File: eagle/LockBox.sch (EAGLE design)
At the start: 12 parts

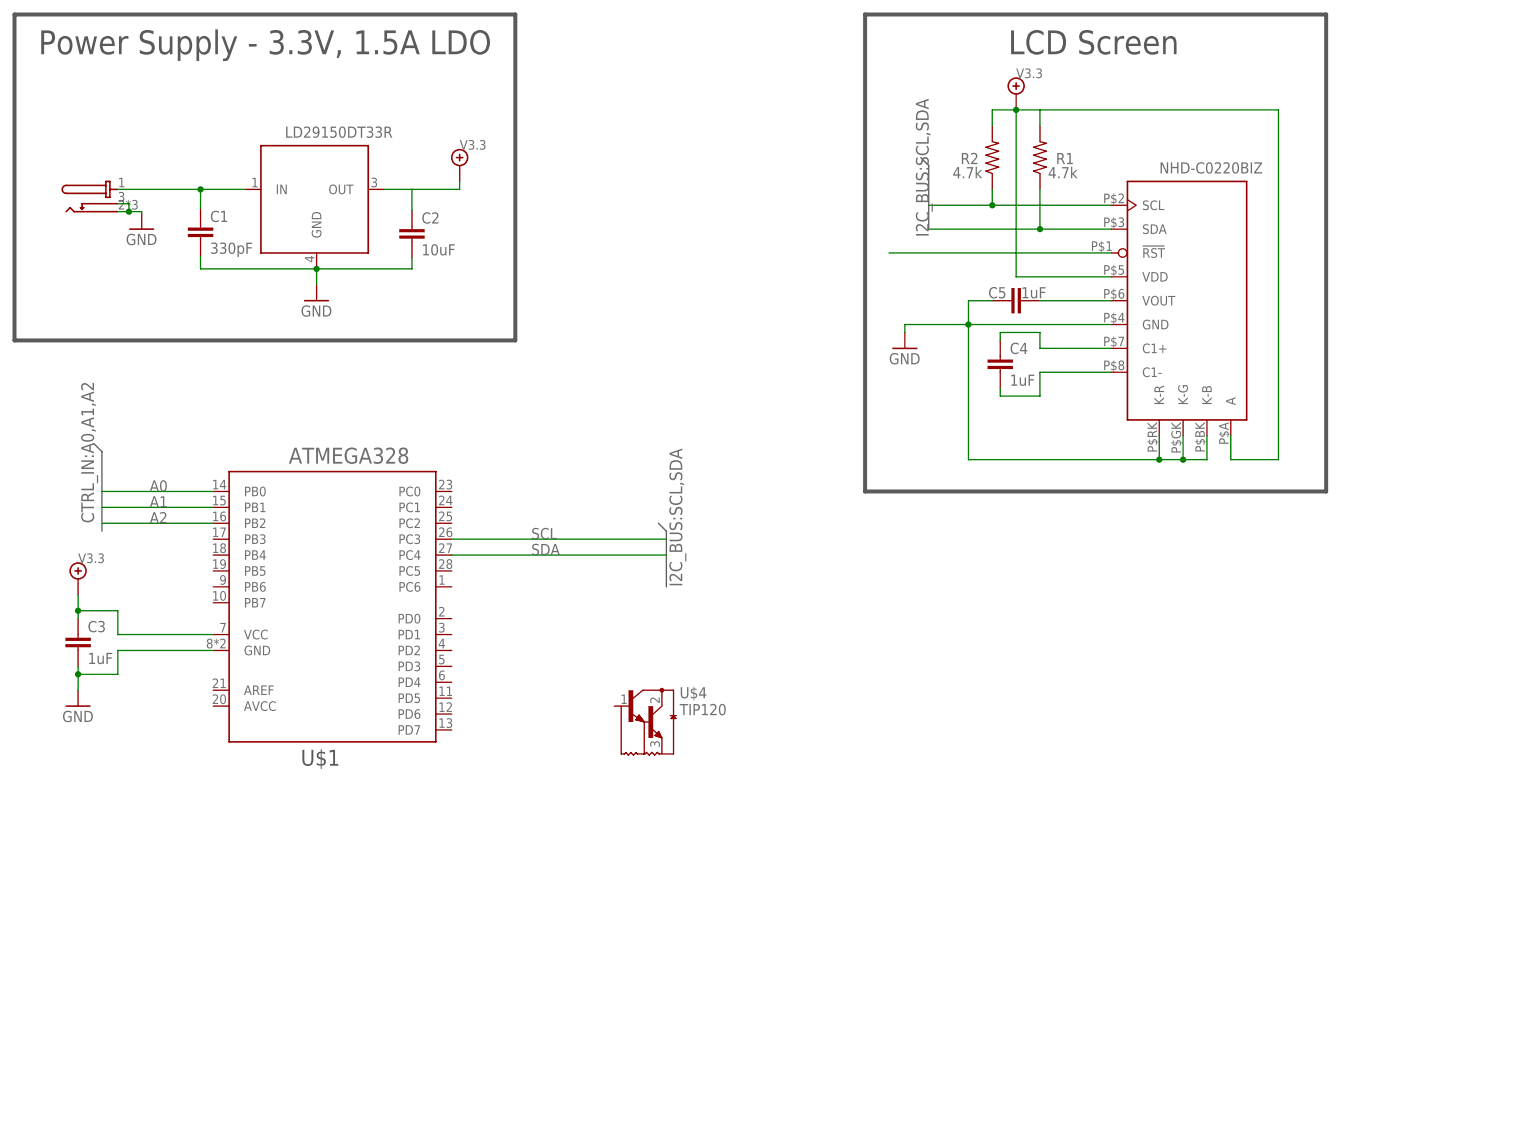
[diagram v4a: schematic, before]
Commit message: Added the TIP120 to LockBox.sch
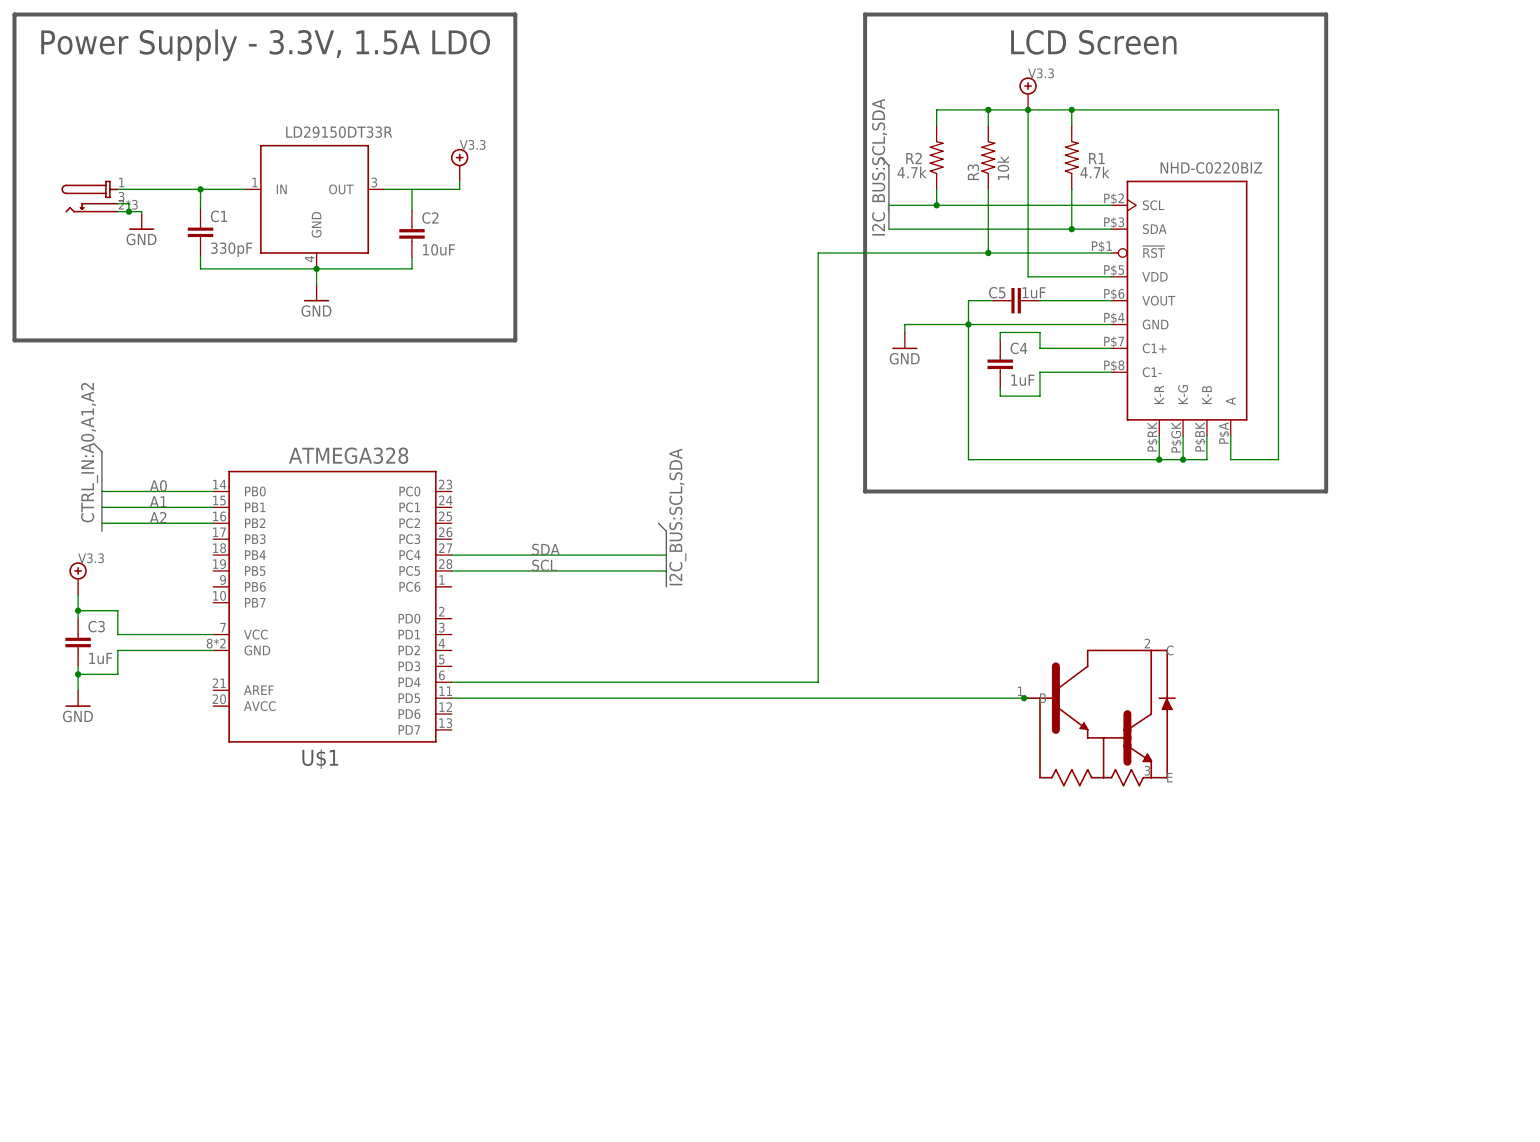
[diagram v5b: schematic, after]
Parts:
- added R3: 10k, LockBox:R-US_M0805
- U$1: PC3 SCL -> (none); PC5 (none) -> SCL; PD4 (none) -> GPIO; PD5 (none) -> GPIO
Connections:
- new net N$8: U$1.PD5, U$4.B
- net N$6: now also R3.1, U$1.PD4
- net P$1: now also R3.2
- net SCL: now also U$1.PC5; no longer U$1.PC3
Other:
- moved on the sheet: R1, R2
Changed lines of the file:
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@@
 <setting verticaltext="up"/>
 </settings>
-<grid distance="0.05" unitdist="inch" unit="inch" style="lines" multiple="1" display="yes" altdistance="0.01" altunitdist="inch" altunit="inch"/>
+<grid distance="0.1" unitdist="inch" unit="inch" style="lines" multiple="1" display="yes" altdistance="0.01" altunitdist="inch" altunit="inch"/>
 <layers>
 <layer number="1" name="Top" color="4" fill="1" visible="no" active="no"/>
@@
 <part name="U$2" library="LockBox" deviceset="LD29150" device="" technology="DT33R"/>
 <part name="U$3" library="LockBox" deviceset="PJ_075" device="" technology="DH"/>
-<part name="U$4" library="LockBox" deviceset="TIP120" device=""/>
 <part name="C1" library="LockBox" deviceset="C" device="" value="330pF"/>
 <part name="C2" library="LockBox" deviceset="C" device="" value="10uF"/>
@@
 <attribute name="PB1" value="GPIO"/>
 <attribute name="PB2" value="GPIO"/>
-<attribute name="PC3" value="SCL"/>
 <attribute name="PC4" value="SDA"/>
+<attribute name="PC5" value="SCL"/>
+<attribute name="PD4" value="GPIO"/>
+<attribute name="PD5" value="GPIO"/>
 </part>
 <part name="C3" library="LockBox" deviceset="C" device="" value="1uF"/>
@@
 <part name="C5" library="LockBox" deviceset="C" device="" value="1uF"/>
 <part name="U$5" library="LockBox" deviceset="NHD-C0220BIZ" device=""/>
+<part name="R3" library="LockBox" deviceset="R-US_" device="M0805" value="10k"/>
+<part name="U$4" library="LockBox" deviceset="TIP120" device=""/>
 </parts>
 <sheets>
@@
 <instance part="U$2" gate="G$1" x="55.88" y="151.13"/>
 <instance part="U$3" gate="G$1" x="26.035" y="151.765"/>
-<instance part="U$4" gate="G$1" x="113.03" y="67.31"/>
 <instance part="C1" gate="G$1" x="41.148" y="146.812"/>
 <instance part="C2" gate="G$1" x="74.93" y="146.558"/>
@@
 <instance part="V1" gate="G1" x="82.55" y="156.21"/>
 <instance part="U$1" gate="G$1" x="62.23" y="88.265">
-<attribute name="PC3" x="62.23" y="88.265" size="1.778" layer="96" display="off"/>
-<attribute name="PC4" x="62.23" y="88.265" size="1.778" layer="96" display="off"/>
 <attribute name="PB0" x="62.23" y="88.265" size="2.032" layer="96" display="off"/>
 <attribute name="PB1" x="62.23" y="88.265" size="2.032" layer="96" display="off"/>
 <attribute name="PB2" x="62.23" y="88.265" size="2.032" layer="96" display="off"/>
+<attribute name="PC4" x="62.23" y="88.265" size="1.778" layer="96" display="off"/>
+<attribute name="PC5" x="62.23" y="88.265" size="1.778" layer="96" display="off"/>
+<attribute name="PD4" x="62.23" y="88.265" size="1.778" layer="96" display="off"/>
+<attribute name="PD5" x="62.23" y="88.265" size="1.778" layer="96" display="off"/>
 </instance>
 <instance part="C3" gate="G$1" x="21.59" y="81.28"/>
@@
 <instance part="V2" gate="G1" x="21.59" y="90.17"/>
 <instance part="C4" gate="G$1" x="168.91" y="125.73"/>
-<instance part="R1" gate="G$1" x="175.26" y="157.48" smashed="yes" rot="R90">
-<attribute name="NAME" x="177.8" y="156.4386" size="1.778" layer="95"/>
-<attribute name="VALUE" x="176.53" y="154.178" size="1.778" layer="96"/>
+<instance part="R1" gate="G$1" x="180.34" y="157.48" smashed="yes" rot="R90">
+<attribute name="NAME" x="182.88" y="156.4386" size="1.778" layer="95"/>
+<attribute name="VALUE" x="181.61" y="154.178" size="1.778" layer="96"/>
 </instance>
-<instance part="R2" gate="G$1" x="167.64" y="157.48" smashed="yes" rot="R90">
-<attribute name="NAME" x="162.56" y="156.4386" size="1.778" layer="95"/>
-<attribute name="VALUE" x="161.29" y="154.178" size="1.778" layer="96"/>
+<instance part="R2" gate="G$1" x="158.75" y="157.48" smashed="yes" rot="R90">
+<attribute name="NAME" x="153.67" y="156.4386" size="1.778" layer="95"/>
+<attribute name="VALUE" x="152.4" y="154.178" size="1.778" layer="96"/>
 </instance>
-<instance part="V3" gate="G1" x="171.45" y="167.64"/>
+<instance part="V3" gate="G1" x="173.355" y="167.64"/>
 <instance part="GND4" gate="1" x="153.67" y="127"/>
 <instance part="C5" gate="G$1" x="170.18" y="134.62" smashed="yes" rot="R90">
@@
 </instance>
 <instance part="U$5" gate="G$1" x="199.39" y="135.89"/>
+<instance part="R3" gate="G$1" x="167.005" y="157.48" rot="R90"/>
+<instance part="U$4" gate="GATE" x="172.72" y="71.12"/>
 </instances>
 <busses>
@@
 </segment>
 <segment>
-<wire x1="156.21" y1="157.48" x2="157.48" y2="156.21" width="0.762" layer="92"/>
-<wire x1="157.48" y1="156.21" x2="157.48" y2="146.05" width="0.762" layer="92"/>
-<label x="157.48" y="144.78" size="2.032" layer="95" rot="R90"/>
+<wire x1="149.86" y1="157.48" x2="151.13" y2="156.21" width="0.762" layer="92"/>
+<wire x1="151.13" y1="156.21" x2="151.13" y2="146.05" width="0.762" layer="92"/>
+<label x="150.495" y="144.78" size="2.032" layer="95" rot="R90"/>
 </segment>
 </bus>
@@
 <segment>
 <pinref part="R2" gate="G$1" pin="2"/>
-<wire x1="167.64" y1="162.56" x2="167.64" y2="165.1" width="0.1524" layer="91"/>
-<wire x1="167.64" y1="165.1" x2="171.45" y2="165.1" width="0.1524" layer="91"/>
+<wire x1="158.75" y1="162.56" x2="158.75" y2="165.1" width="0.1524" layer="91"/>
+<wire x1="158.75" y1="165.1" x2="167.005" y2="165.1" width="0.1524" layer="91"/>
 <pinref part="R1" gate="G$1" pin="2"/>
-<wire x1="171.45" y1="165.1" x2="175.26" y2="165.1" width="0.1524" layer="91"/>
-<wire x1="175.26" y1="165.1" x2="175.26" y2="162.56" width="0.1524" layer="91"/>
+<wire x1="167.005" y1="165.1" x2="173.355" y2="165.1" width="0.1524" layer="91"/>
+<wire x1="173.355" y1="165.1" x2="180.34" y2="165.1" width="0.1524" layer="91"/>
+<wire x1="180.34" y1="165.1" x2="180.34" y2="162.56" width="0.1524" layer="91"/>
 <pinref part="V3" gate="G1" pin="P$1"/>
-<junction x="171.45" y="165.1"/>
+<junction x="173.355" y="165.1"/>
 <pinref part="U$5" gate="G$1" pin="VDD"/>
-<wire x1="186.69" y1="138.43" x2="171.45" y2="138.43" width="0.1524" layer="91"/>
-<wire x1="171.45" y1="138.43" x2="171.45" y2="165.1" width="0.1524" layer="91"/>
-<wire x1="175.26" y1="165.1" x2="213.36" y2="165.1" width="0.1524" layer="91"/>
+<wire x1="186.69" y1="138.43" x2="173.355" y2="138.43" width="0.1524" layer="91"/>
+<wire x1="173.355" y1="138.43" x2="173.355" y2="165.1" width="0.1524" layer="91"/>
+<wire x1="180.34" y1="165.1" x2="213.36" y2="165.1" width="0.1524" layer="91"/>
 <wire x1="213.36" y1="165.1" x2="213.36" y2="109.22" width="0.1524" layer="91"/>
 <wire x1="213.36" y1="109.22" x2="205.74" y2="109.22" width="0.1524" layer="91"/>
 <pinref part="U$5" gate="G$1" pin="A"/>
 <wire x1="205.74" y1="109.22" x2="205.74" y2="113.03" width="0.1524" layer="91"/>
+<pinref part="R3" gate="G$1" pin="2"/>
+<wire x1="167.005" y1="162.56" x2="167.005" y2="165.1" width="0.1524" layer="91"/>
+<junction x="167.005" y="165.1"/>
+<junction x="180.34" y="165.1"/>
 </segment>
 </net>
 <net name="SCL" class="0">
 <segment>
-<pinref part="U$1" gate="G$1" pin="PC3"/>
-<wire x1="115.57" y1="96.52" x2="81.28" y2="96.52" width="0.1524" layer="91"/>
-<label x="93.98" y="96.52" size="1.778" layer="95"/>
-</segment>
-<segment>
-<wire x1="157.48" y1="149.86" x2="167.64" y2="149.86" width="0.1524" layer="91"/>
+<wire x1="151.13" y1="149.86" x2="158.75" y2="149.86" width="0.1524" layer="91"/>
 <pinref part="R2" gate="G$1" pin="1"/>
-<wire x1="167.64" y1="149.86" x2="167.64" y2="152.4" width="0.1524" layer="91"/>
-<wire x1="167.64" y1="149.86" x2="186.69" y2="149.86" width="0.1524" layer="91"/>
-<junction x="167.64" y="149.86"/>
+<wire x1="158.75" y1="149.86" x2="158.75" y2="152.4" width="0.1524" layer="91"/>
+<wire x1="158.75" y1="149.86" x2="186.69" y2="149.86" width="0.1524" layer="91"/>
+<junction x="158.75" y="149.86"/>
 <pinref part="U$5" gate="G$1" pin="SCL"/>
 </segment>
+<segment>
+<pinref part="U$1" gate="G$1" pin="PC5"/>
+<wire x1="115.57" y1="91.44" x2="81.28" y2="91.44" width="0.1524" layer="91"/>
+<label x="93.98" y="91.44" size="1.778" layer="95"/>
+</segment>
 </net>
 <net name="SDA" class="0">
+<segment>
+<wire x1="151.13" y1="146.05" x2="180.34" y2="146.05" width="0.1524" layer="91"/>
+<pinref part="R1" gate="G$1" pin="1"/>
+<wire x1="180.34" y1="146.05" x2="180.34" y2="152.4" width="0.1524" layer="91"/>
+<wire x1="180.34" y1="146.05" x2="186.69" y2="146.05" width="0.1524" layer="91"/>
+<junction x="180.34" y="146.05"/>
+<pinref part="U$5" gate="G$1" pin="SDA"/>
+</segment>
 <segment>
 <pinref part="U$1" gate="G$1" pin="PC4"/>
 <wire x1="115.57" y1="93.98" x2="81.28" y2="93.98" width="0.1524" layer="91"/>
 <label x="93.98" y="93.98" size="1.778" layer="95"/>
-</segment>
-<segment>
-<wire x1="157.48" y1="146.05" x2="175.26" y2="146.05" width="0.1524" layer="91"/>
-<pinref part="R1" gate="G$1" pin="1"/>
-<wire x1="175.26" y1="146.05" x2="175.26" y2="152.4" width="0.1524" layer="91"/>
-<wire x1="175.26" y1="146.05" x2="186.69" y2="146.05" width="0.1524" layer="91"/>
-<junction x="175.26" y="146.05"/>
-<pinref part="U$5" gate="G$1" pin="SDA"/>
 </segment>
 </net>
@@
 <segment>
 <pinref part="U$5" gate="G$1" pin="!RST"/>
-<wire x1="186.69" y1="142.24" x2="151.13" y2="142.24" width="0.1524" layer="91"/>
-</segment>
-</net>
+<wire x1="186.69" y1="142.24" x2="167.005" y2="142.24" width="0.1524" layer="91"/>
+<pinref part="U$1" gate="G$1" pin="PD4"/>
+<wire x1="167.005" y1="142.24" x2="139.827" y2="142.24" width="0.1524" layer="91"/>
+<wire x1="81.28" y1="73.66" x2="139.827" y2="73.66" width="0.1524" layer="91"/>
+<wire x1="139.827" y1="73.66" x2="139.827" y2="142.24" width="0.1524" layer="91"/>
+<junction x="167.005" y="142.24"/>
+<pinref part="R3" gate="G$1" pin="1"/>
+<wire x1="167.005" y1="142.24" x2="167.005" y2="152.4" width="0.1524" layer="91"/>
+</segment>
+</net>
+<net name="N$8" class="0">
+<segment>
+<pinref part="U$1" gate="G$1" pin="PD5"/>
+<wire x1="81.28" y1="71.12" x2="172.72" y2="71.12" width="0.1524" layer="91"/>
+<pinref part="U$4" gate="GATE" pin="B"/>
+<wire x1="172.72" y1="71.12" x2="173.4058" y2="71.12" width="0.1524" layer="91"/>
+<junction x="172.72" y="71.12"/>
+</segment>
+</net>

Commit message: Added 2pin header and 12V supply symbol to LockBox.lbr
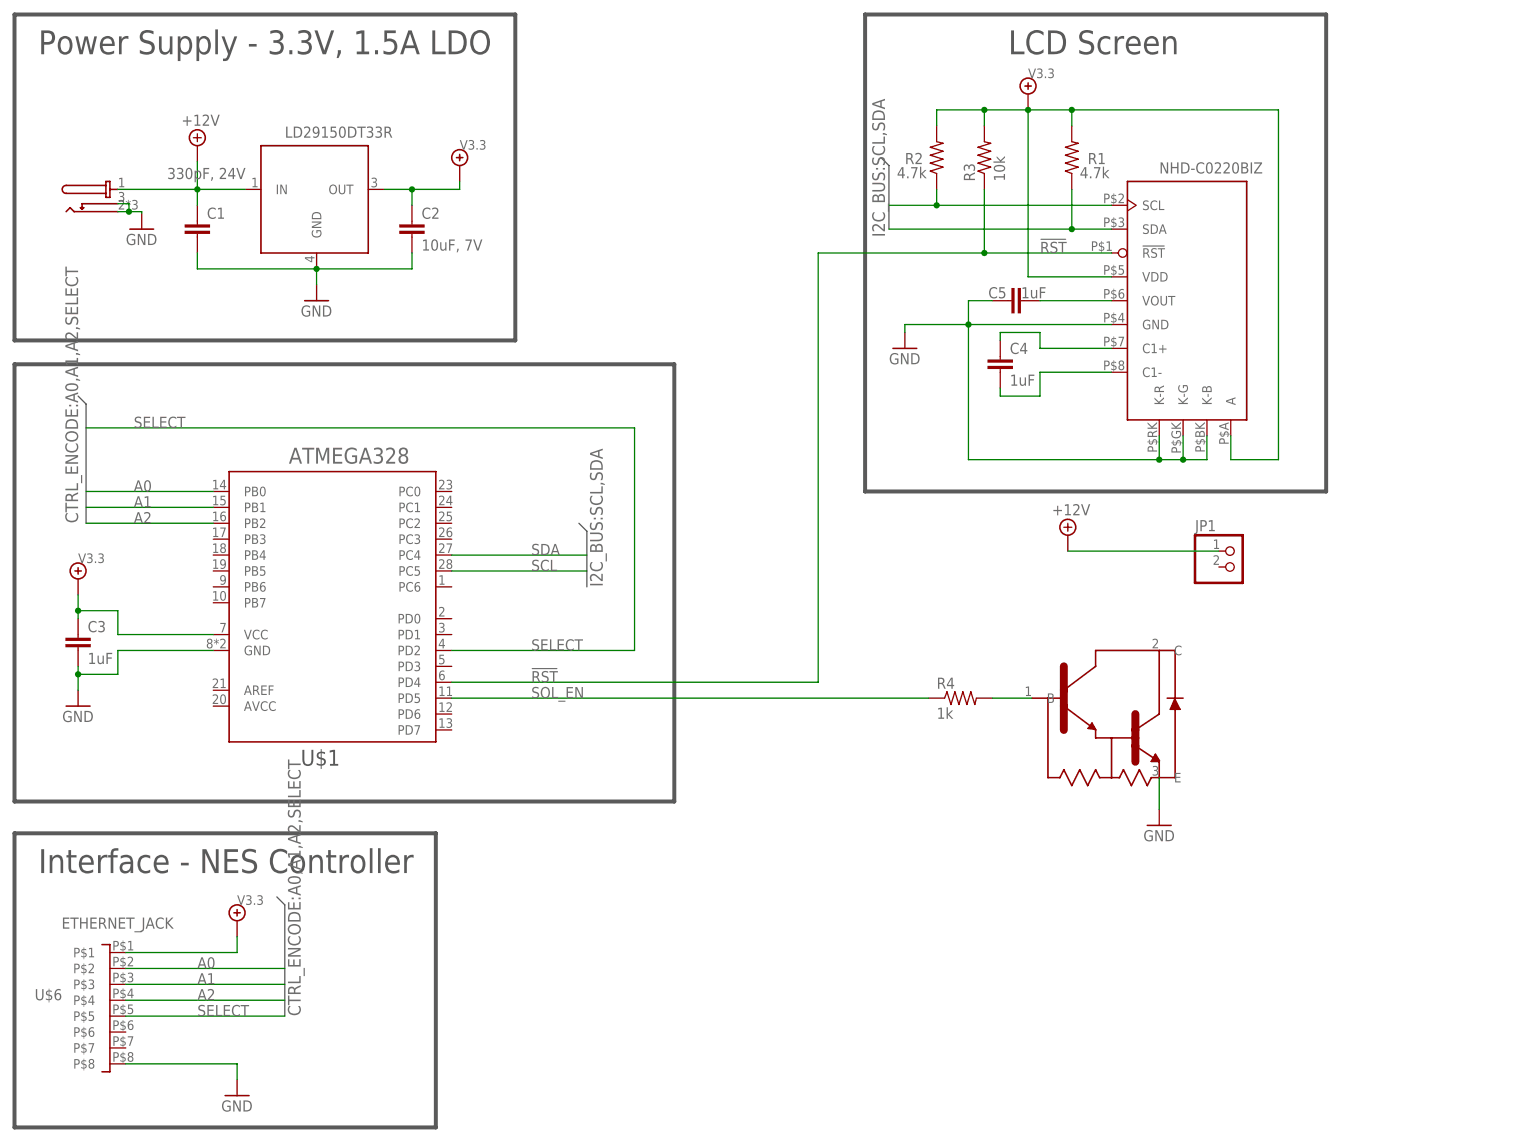
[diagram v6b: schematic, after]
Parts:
- added JP1: (no value), LockBox:PINHD-1X2
- added R4: 1k, LockBox:R-US_M0805
- added U$6: ETHERNET_JACK, LockBox:ETHERNET_JACK
- C1: value 330pF -> 330pF, 24V
- C2: value 10uF -> 10uF, 7V
- U$1: PD2 (none) -> INT0
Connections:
- net N$6 renamed !RST
- removed net N$1: C1.1, U$2.IN, U$3.PWR
- removed net N$8: U$1.PD5, U$4.B
- new net +12V: C1.1, JP1.1, U$2.IN, U$3.PWR
- new net SELECT: U$1.PD2, U$6.P$5
- new net SOL_EN: R4.1, R4.2, U$1.PD5, U$4.B
- net A0: now also U$6.P$2
- net A1: now also U$6.P$3
- net A2: now also U$6.P$4
- net GND: now also U$4.E, U$6.P$8
- net P$1: now also U$6.P$1
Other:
- note added: "Interface - NES Controller"
- moved on the sheet: C1, C2, R3
